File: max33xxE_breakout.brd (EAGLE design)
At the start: 50 x 50 mm, 16 parts

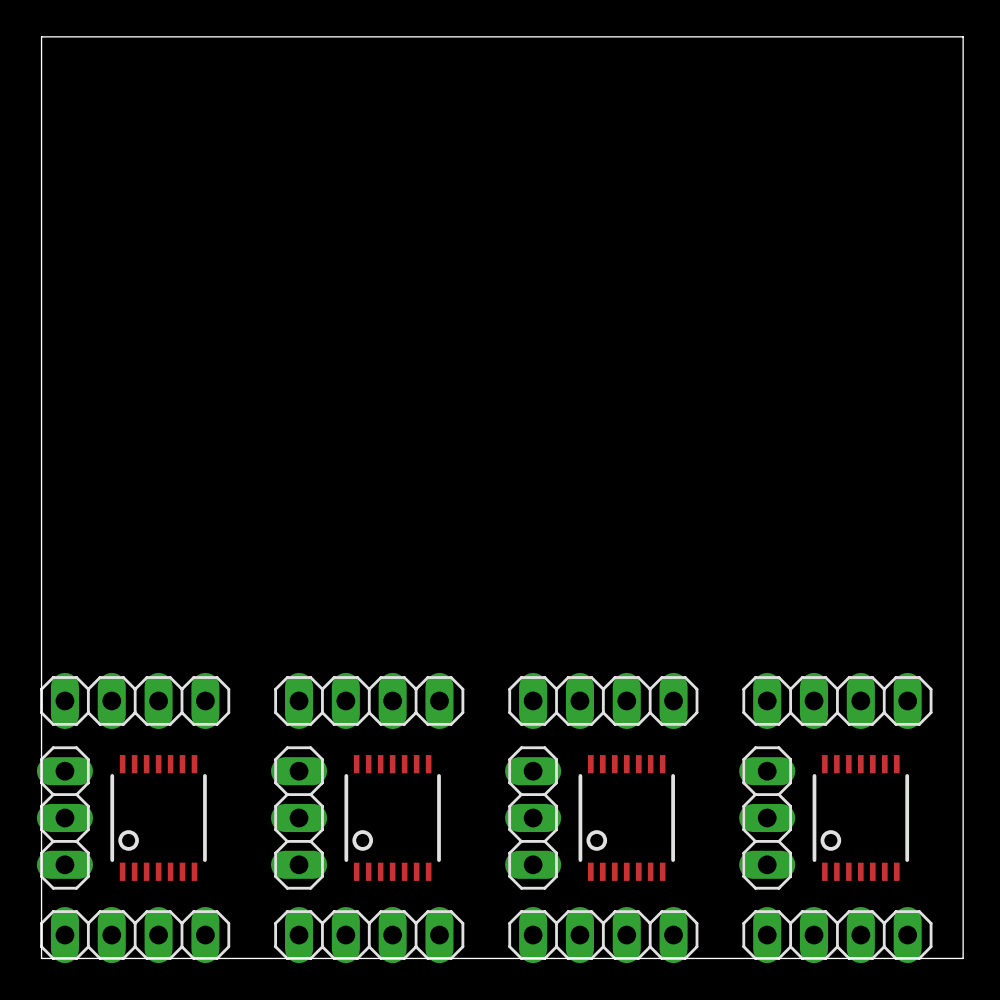
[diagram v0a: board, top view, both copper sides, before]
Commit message: size down the board
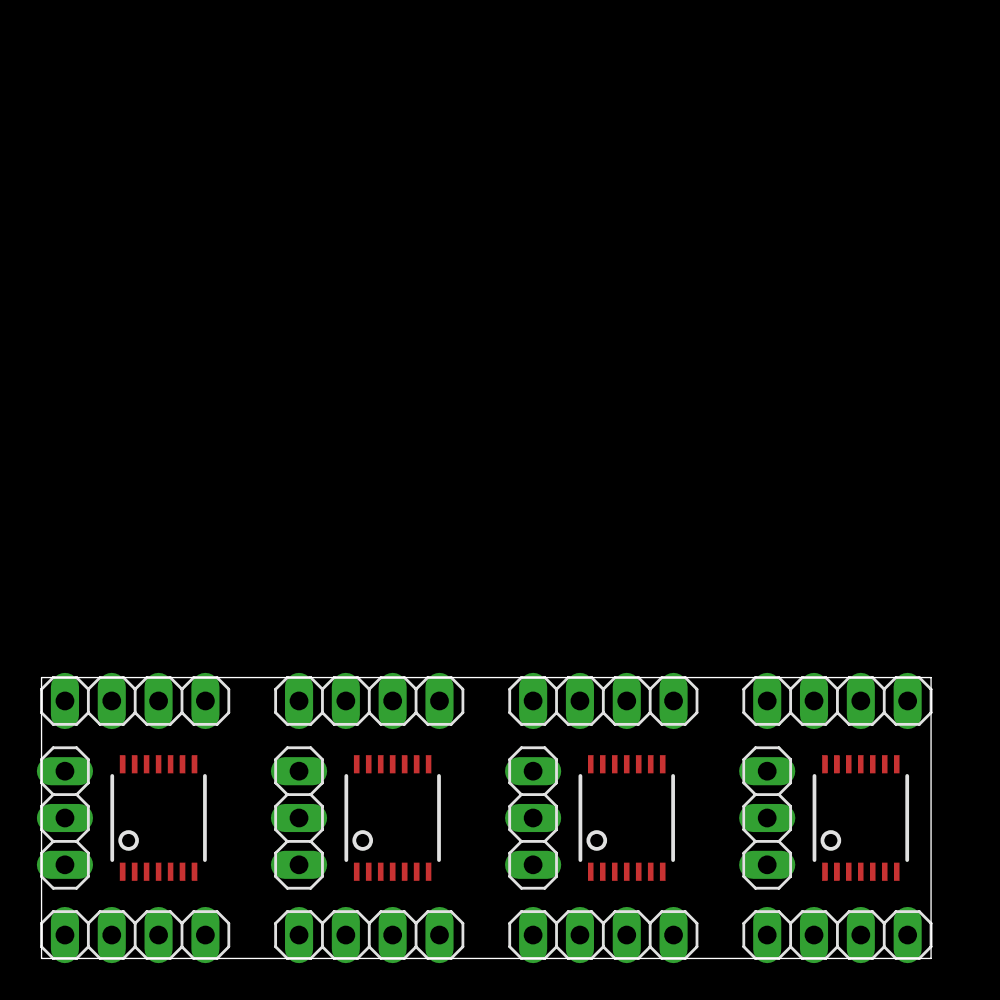
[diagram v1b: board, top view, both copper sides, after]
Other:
- board size 50 x 50 mm -> 48.3 x 15.2 mm
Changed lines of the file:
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@@
 <board>
 <plain>
-<wire x1="0" y1="0" x2="50" y2="0" width="0" layer="20"/>
-<wire x1="50" y1="0" x2="50" y2="50" width="0" layer="20"/>
-<wire x1="50" y1="50" x2="0" y2="50" width="0" layer="20"/>
-<wire x1="0" y1="50" x2="0" y2="0" width="0" layer="20"/>
+<wire x1="0" y1="0" x2="48.26" y2="0" width="0" layer="20"/>
+<wire x1="48.26" y1="0" x2="48.26" y2="15.24" width="0" layer="20"/>
+<wire x1="48.26" y1="15.24" x2="0" y2="15.24" width="0" layer="20"/>
+<wire x1="0" y1="15.24" x2="0" y2="0" width="0" layer="20"/>
 </plain>
 <attributes>

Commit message: bypass caps
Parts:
- added C1, C2, C3, C4, C5, C6, C7, C8: (no value), rcl:C0603K
- moved SHIFT1 0.64 mm to (6.99, 7.62)
- moved SHIFT2 0.63 mm to (19.7, 7.62)
- moved SHIFT3 0.63 mm to (32.4, 7.62)
- moved SHIFT4 0.63 mm to (45.1, 7.62)
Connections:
- net GND: now also C1.2, C2.2, C3.2, C4.2, C5.2, C6.2, C7.2, C8.2
- net VCC_SHIFT1: now also C2.1
- net VCC_SHIFT2: now also C4.1
- net VCC_SHIFT3: now also C6.1
- net VCC_SHIFT4: now also C8.1
- net VL_SHIFT1: now also C1.1
- net VL_SHIFT2: now also C3.1
- net VL_SHIFT3: now also C5.1
- net VL_SHIFT4: now also C7.1

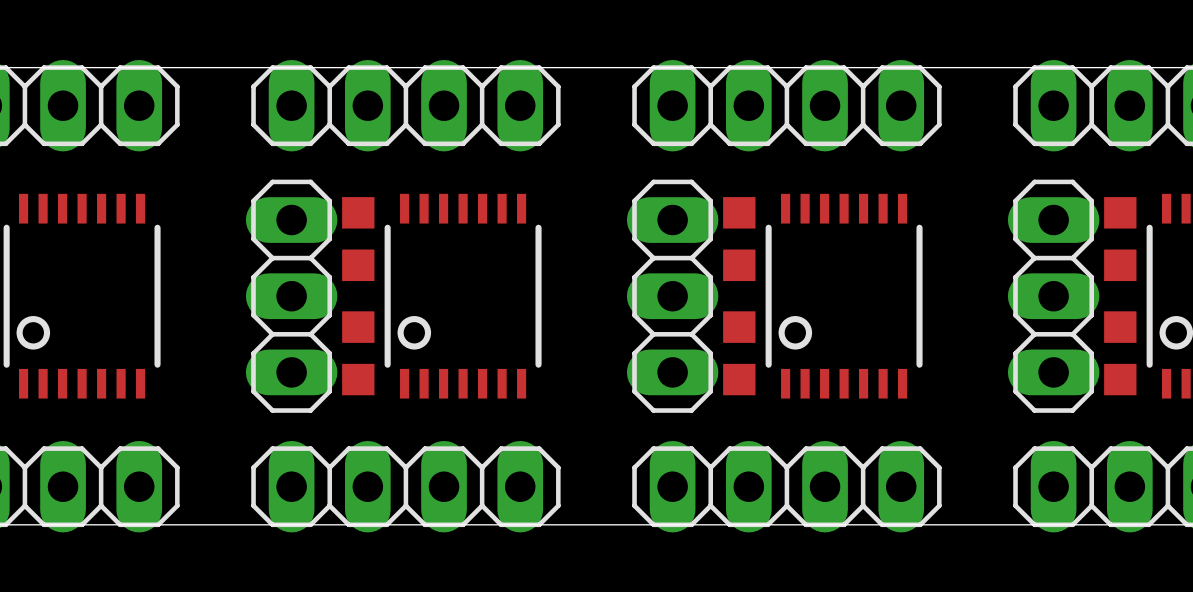
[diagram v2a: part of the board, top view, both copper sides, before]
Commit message: join the separate VCC and VL segments with solderpads
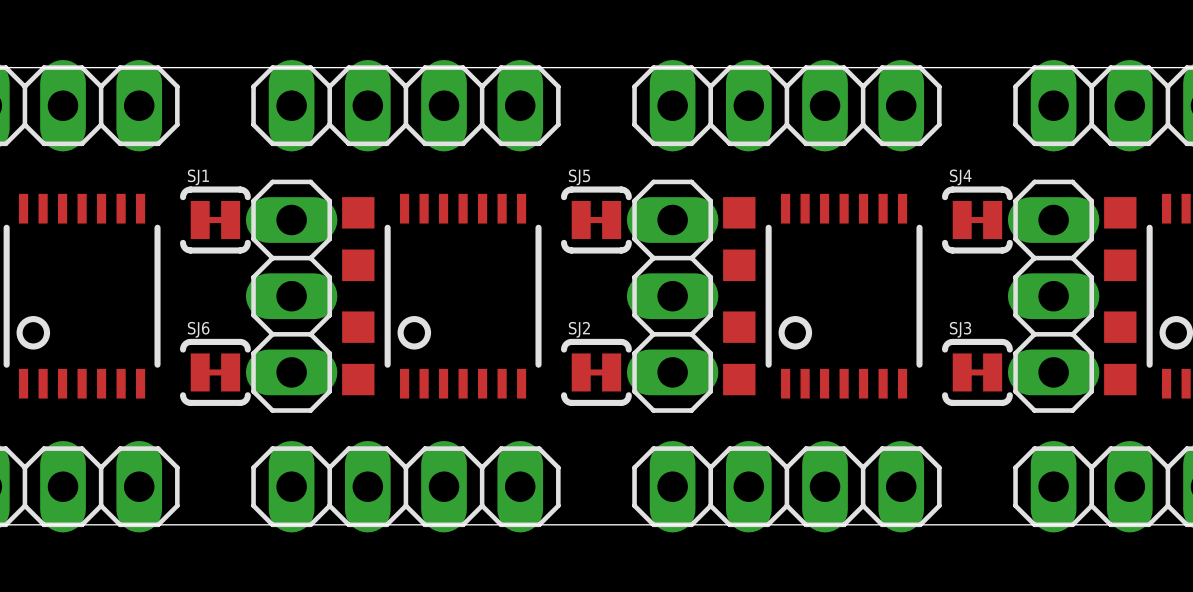
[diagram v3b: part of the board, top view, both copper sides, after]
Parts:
- added SJ1, SJ2, SJ3, SJ4, SJ5, SJ6: SOLDERJUMPERTRACE, SparkFun-Passives:SJ_2S-TRACE
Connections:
- net VCC_SHIFT1: now also SJ1.1
- net VCC_SHIFT2: now also SJ1.2, SJ5.1
- net VCC_SHIFT3: now also SJ4.1, SJ5.2
- net VCC_SHIFT4: now also SJ4.2
- net VL_SHIFT1: now also SJ6.1
- net VL_SHIFT2: now also SJ2.1, SJ6.2
- net VL_SHIFT3: now also SJ2.2, SJ3.1
- net VL_SHIFT4: now also SJ3.2
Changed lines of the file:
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@@
 <layer number="111" name="MPL" color="7" fill="1" visible="yes" active="yes"/>
 <layer number="112" name="tSilk" color="7" fill="1" visible="yes" active="yes"/>
+<layer number="116" name="Patch_BOT" color="9" fill="4" visible="no" active="yes"/>
 <layer number="121" name="sName" color="7" fill="1" visible="yes" active="yes"/>
 <layer number="122" name="_bPlace" color="7" fill="1" visible="yes" active="yes"/>
@@
 <layer number="204" name="204bmp" color="7" fill="1" visible="yes" active="yes"/>
 <layer number="205" name="205bmp" color="7" fill="1" visible="yes" active="yes"/>
+<layer number="206" name="206bmp" color="7" fill="10" visible="no" active="yes"/>
+<layer number="207" name="207bmp" color="8" fill="10" visible="no" active="yes"/>
+<layer number="208" name="208bmp" color="9" fill="10" visible="no" active="yes"/>
+<layer number="209" name="209bmp" color="7" fill="1" visible="no" active="yes"/>
+<layer number="210" name="210bmp" color="7" fill="1" visible="no" active="yes"/>
+<layer number="211" name="211bmp" color="7" fill="1" visible="no" active="yes"/>
+<layer number="212" name="212bmp" color="7" fill="1" visible="no" active="yes"/>
+<layer number="213" name="213bmp" color="7" fill="1" visible="no" active="yes"/>
+<layer number="214" name="214bmp" color="7" fill="1" visible="no" active="yes"/>
+<layer number="215" name="215bmp" color="7" fill="1" visible="no" active="yes"/>
+<layer number="216" name="216bmp" color="7" fill="1" visible="no" active="yes"/>
+<layer number="217" name="217bmp" color="18" fill="1" visible="no" active="no"/>
+<layer number="218" name="218bmp" color="19" fill="1" visible="no" active="no"/>
+<layer number="219" name="219bmp" color="20" fill="1" visible="no" active="no"/>
+<layer number="220" name="220bmp" color="21" fill="1" visible="no" active="no"/>
+<layer number="221" name="221bmp" color="22" fill="1" visible="no" active="no"/>
+<layer number="222" name="222bmp" color="23" fill="1" visible="no" active="no"/>
+<layer number="223" name="223bmp" color="24" fill="1" visible="no" active="no"/>
+<layer number="224" name="224bmp" color="25" fill="1" visible="no" active="no"/>
 <layer number="248" name="Housing" color="7" fill="1" visible="yes" active="yes"/>
 <layer number="249" name="Edge" color="7" fill="1" visible="yes" active="yes"/>
@@
 <attribute name="VALUE" x="39.9425" y="10.325" size="1.016" layer="27" rot="R270"/>
 </element>
+<element name="SJ1" library="SparkFun-Passives" package="SJ_2S-TRACE" value="SOLDERJUMPERTRACE" x="11.43" y="10.16"/>
+<element name="SJ2" library="SparkFun-Passives" package="SJ_2S-TRACE" value="SOLDERJUMPERTRACE" x="24.13" y="5.08"/>
+<element name="SJ3" library="SparkFun-Passives" package="SJ_2S-TRACE" value="SOLDERJUMPERTRACE" x="36.83" y="5.08"/>
+<element name="SJ4" library="SparkFun-Passives" package="SJ_2S-TRACE" value="SOLDERJUMPERTRACE" x="36.83" y="10.16"/>
+<element name="SJ5" library="SparkFun-Passives" package="SJ_2S-TRACE" value="SOLDERJUMPERTRACE" x="24.13" y="10.16"/>
+<element name="SJ6" library="SparkFun-Passives" package="SJ_2S-TRACE" value="SOLDERJUMPERTRACE" x="11.43" y="5.08"/>
 </elements>
 <signals>
@@
 <contactref element="PWR_SHIFT1" pad="1"/>
 <contactref element="C2" pad="1"/>
+<contactref element="SJ1" pad="1"/>
+<wire x1="5.035" y1="10.5378" x2="10.922" y2="10.16" width="0" layer="19" extent="1-1"/>
 <wire x1="3.4925" y1="10.4" x2="5.035" y2="10.5378" width="0" layer="19" extent="1-1"/>
 <wire x1="1.27" y1="10.16" x2="3.4925" y2="10.4" width="0" layer="19" extent="1-1"/>
@@
 <contactref element="PWR_SHIFT1" pad="3"/>
 <contactref element="C1" pad="1"/>
+<contactref element="SJ6" pad="1"/>
+<wire x1="5.035" y1="4.7022" x2="10.922" y2="5.08" width="0" layer="19" extent="1-1"/>
 <wire x1="3.4925" y1="4.84" x2="5.035" y2="4.7022" width="0" layer="19" extent="1-1"/>
 <wire x1="1.27" y1="5.08" x2="3.4925" y2="4.84" width="0" layer="19" extent="1-1"/>
@@
 <contactref element="PWR_SHIFT2" pad="3"/>
 <contactref element="C3" pad="1"/>
+<contactref element="SJ6" pad="2"/>
+<contactref element="SJ2" pad="1"/>
+<wire x1="17.735" y1="4.7022" x2="23.622" y2="5.08" width="0" layer="19" extent="1-1"/>
 <wire x1="16.1925" y1="4.84" x2="17.735" y2="4.7022" width="0" layer="19" extent="1-1"/>
 <wire x1="13.97" y1="5.08" x2="16.1925" y2="4.84" width="0" layer="19" extent="1-1"/>
+<wire x1="11.938" y1="5.08" x2="13.97" y2="5.08" width="0" layer="19" extent="1-1"/>
 </signal>
 <signal name="VCC_SHIFT2">
@@
 <contactref element="PWR_SHIFT2" pad="1"/>
 <contactref element="C4" pad="1"/>
+<contactref element="SJ1" pad="2"/>
+<contactref element="SJ5" pad="1"/>
+<wire x1="17.735" y1="10.5378" x2="23.622" y2="10.16" width="0" layer="19" extent="1-1"/>
 <wire x1="16.1925" y1="10.4" x2="17.735" y2="10.5378" width="0" layer="19" extent="1-1"/>
 <wire x1="13.97" y1="10.16" x2="16.1925" y2="10.4" width="0" layer="19" extent="1-1"/>
+<wire x1="11.938" y1="10.16" x2="13.97" y2="10.16" width="0" layer="19" extent="1-1"/>
 </signal>
 <signal name="IOVCC4_SHIFT3">
@@
 <contactref element="PWR_SHIFT3" pad="3"/>
 <contactref element="C5" pad="1"/>
+<contactref element="SJ3" pad="1"/>
+<contactref element="SJ2" pad="2"/>
+<wire x1="30.435" y1="4.7022" x2="36.322" y2="5.08" width="0" layer="19" extent="1-1"/>
 <wire x1="28.8925" y1="4.84" x2="30.435" y2="4.7022" width="0" layer="19" extent="1-1"/>
 <wire x1="26.67" y1="5.08" x2="28.8925" y2="4.84" width="0" layer="19" extent="1-1"/>
+<wire x1="24.638" y1="5.08" x2="26.67" y2="5.08" width="0" layer="19" extent="1-1"/>
 </signal>
 <signal name="VCC_SHIFT3">
@@
 <contactref element="PWR_SHIFT3" pad="1"/>
 <contactref element="C6" pad="1"/>
+<contactref element="SJ4" pad="1"/>
+<contactref element="SJ5" pad="2"/>
+<wire x1="30.435" y1="10.5378" x2="36.322" y2="10.16" width="0" layer="19" extent="1-1"/>
 <wire x1="28.8925" y1="10.4" x2="30.435" y2="10.5378" width="0" layer="19" extent="1-1"/>
 <wire x1="26.67" y1="10.16" x2="28.8925" y2="10.4" width="0" layer="19" extent="1-1"/>
+<wire x1="24.638" y1="10.16" x2="26.67" y2="10.16" width="0" layer="19" extent="1-1"/>
 </signal>
 <signal name="IOVCC4_SHIFT4">
@@
 <contactref element="PWR_SHIFT4" pad="3"/>
 <contactref element="C7" pad="1"/>
+<contactref element="SJ3" pad="2"/>
 <wire x1="41.5925" y1="4.84" x2="43.135" y2="4.7022" width="0" layer="19" extent="1-1"/>
 <wire x1="39.37" y1="5.08" x2="41.5925" y2="4.84" width="0" layer="19" extent="1-1"/>
+<wire x1="37.338" y1="5.08" x2="39.37" y2="5.08" width="0" layer="19" extent="1-1"/>
 </signal>
 <signal name="VCC_SHIFT4">
@@
 <contactref element="PWR_SHIFT4" pad="1"/>
 <contactref element="C8" pad="1"/>
+<contactref element="SJ4" pad="2"/>
 <wire x1="41.5925" y1="10.4" x2="43.135" y2="10.5378" width="0" layer="19" extent="1-1"/>
 <wire x1="39.37" y1="10.16" x2="41.5925" y2="10.4" width="0" layer="19" extent="1-1"/>
+<wire x1="37.338" y1="10.16" x2="39.37" y2="10.16" width="0" layer="19" extent="1-1"/>
 </signal>
 </signals>
